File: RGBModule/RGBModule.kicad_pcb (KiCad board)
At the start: 2 copper layers, 17.8 x 24.4 mm, 9 parts, among them P1 CONN_01X03, SW1 Pulsador, SW2 Final_carrera

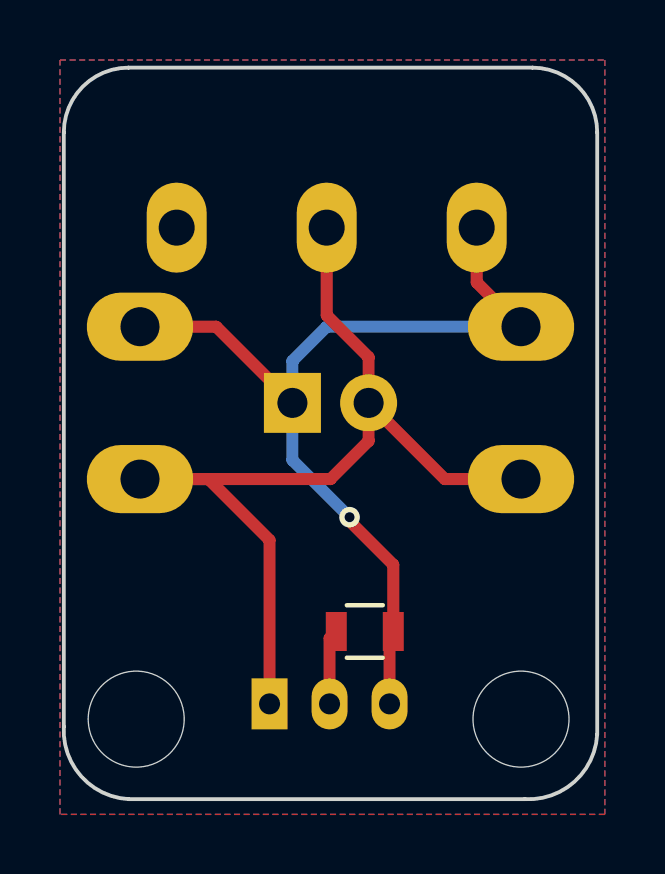
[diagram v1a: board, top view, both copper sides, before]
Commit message: 3D terminado
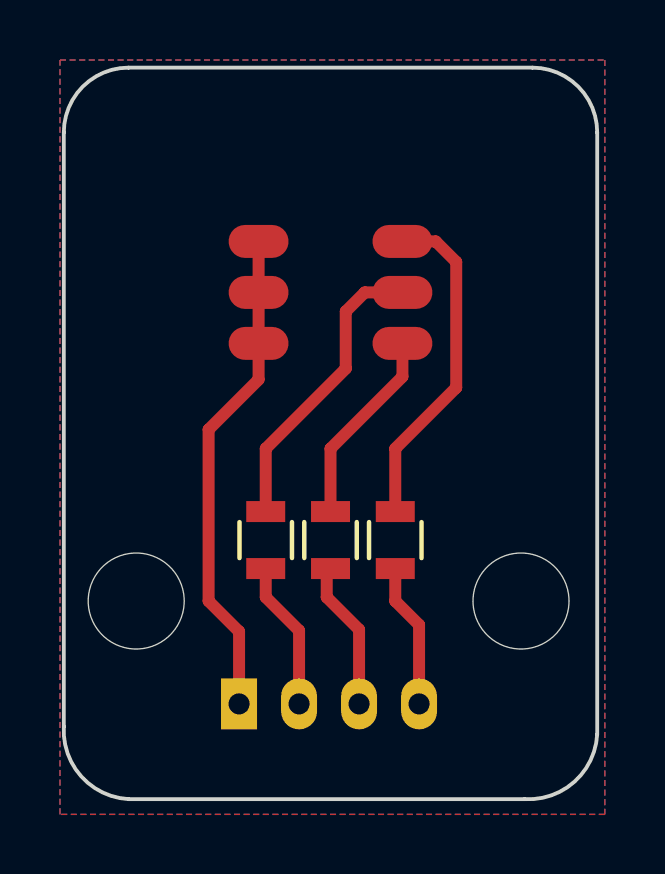
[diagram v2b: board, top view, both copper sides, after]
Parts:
- removed G***: LOGO, logos_frizzy:glance
- removed G***: LOGO, logos_frizzy:web
- removed the REF** at (144.3, 111.9)
- removed the REF** at (131.4, 111.9)
- removed SW1: Pulsador, Buttons_Switches_THT:SW_PUSH-12mm
- removed SW2: Final_carrera, frizzy_switches:limit_sw_tiaihua
- added LED1: RGBLED5050, SparkFun-LED:LED-TRICOLOR-5050, F.Cu at (137.9, 97.7)
- added R3: 470, Resistors_SMD:R_0805, F.Cu at (135.8, 105.9)
- added REF**: MountingHole_3.2mm_M3, Mounting_Holes:MountingHole_3.2mm_M3, F.Cu at (144.3, 108.0)
- added REF**: MountingHole_3.2mm_M3, Mounting_Holes:MountingHole_3.2mm_M3, F.Cu at (131.4, 108.0)
- P1: value CONN_01X03 -> CONN_01X04; footprint Connectors_JST:JST_PH_S3B-PH-K_03x2.00mm_Angled -> Connectors_JST:JST_PH_S4B-PH-K_04x2.00mm_Angled
- R1: value 10k -> 330
- R2: value R_PHOTO -> 330; footprint LEDs:LED-5MM -> Resistors_SMD:R_0805
- moved R2 4.75 mm to (137.9, 105.9), turned to 270 degrees
- moved R1 3.21 mm to (140.1, 105.9), turned to 90 degrees
- moved P1 1.02 mm to (134.9, 111.4)
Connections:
- P1 pad 2: 5V -> RED
- P1 pad 3: SIGNAL -> GREEN
- R1 pad 1: 5V -> BLUE
- R1 pad 2: SIGNAL -> Net-(LED1-Pad3)
- R2 pad 1: SIGNAL -> Net-(LED1-Pad1)
- R2 pad 2: GND -> GREEN
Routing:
- net SIGNAL: track 31.2 -> 0.00 mm, vias 1 -> 0
- net GND: track 33.2 -> 16.5 mm
- net Net-(LED1-Pad3): track 0.00 -> 11.2 mm
- net Net-(LED1-Pad2): track 0.00 -> 9.93 mm
- net Net-(LED1-Pad1): track 0.00 -> 6.60 mm
- net GREEN: track 0.00 -> 5.01 mm
- net RED: track 0.00 -> 4.97 mm
- net BLUE: track 0.00 -> 4.84 mm
- net 5V: track 2.98 -> 0.00 mm

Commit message: Serigrafia añadida
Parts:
- added G***: LOGO, Buzzers_Beepers:logo_rgb, B.Cu at (137.8, 98.4)

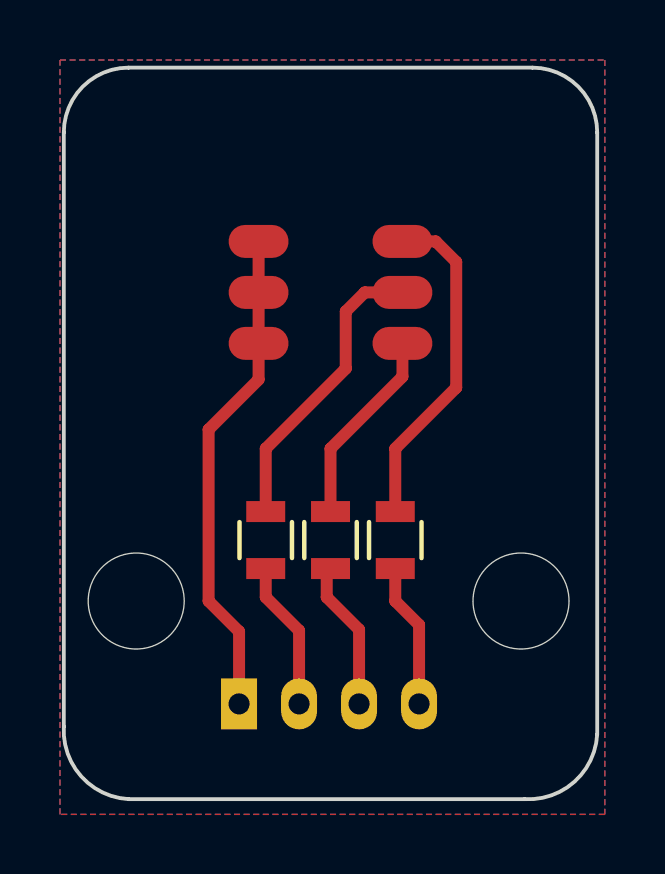
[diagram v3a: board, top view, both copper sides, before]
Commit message: Añadida la serigrafia en la conexiones
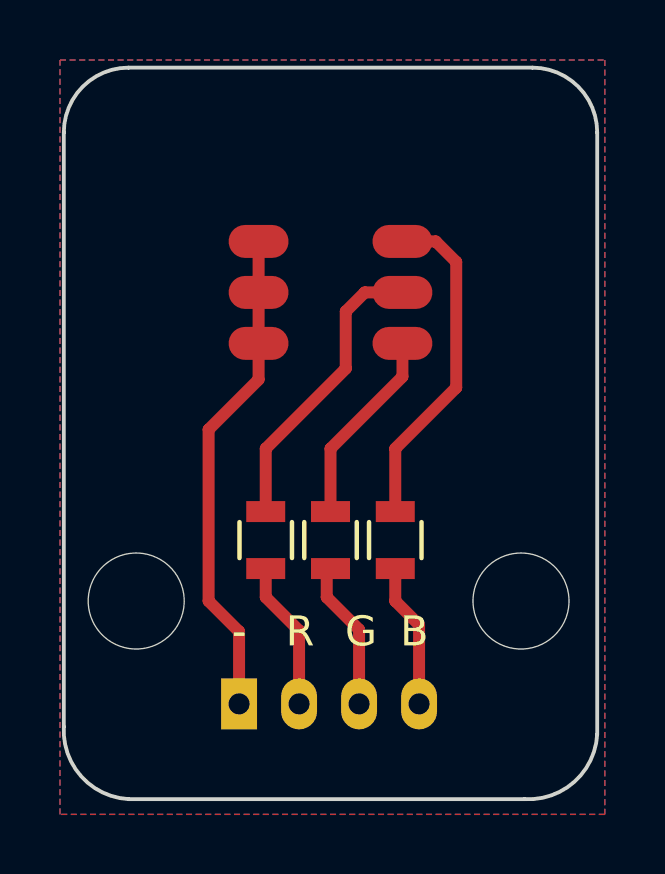
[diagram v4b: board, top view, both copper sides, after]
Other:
- board text added: "-"
- board text added: "B"
- board text added: "G"
- board text added: "R"
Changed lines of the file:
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@@
 (kicad_pcb (version 4) (host pcbnew 4.0.4-stable)
   (general
-    (links 0)
+    (links 9)
     (no_connects 0)
     (area 128.964974 90.106499 146.875501 114.621026)
     (thickness 1.6)
-    (drawings 15)
+    (drawings 19)
     (tracks 30)
     (zones 0)
@@
       (xy -2.827142 5.865992) (xy -2.687518 5.867258) (xy -2.579421 5.867472) (xy -2.074333 5.867258)) (layer B.SilkS) (width 0.01))
   )
+  (gr_text "-\n" (at 134.874 108.966) (layer F.SilkS)
+    (effects (font (size 1 1) (thickness 0.25)))
+  )
+  (gr_text B (at 140.716 108.966) (layer F.SilkS)
+    (effects (font (size 1 1) (thickness 0.25)))
+  )
+  (gr_text "G\n" (at 138.938 108.966) (layer F.SilkS)
+    (effects (font (size 1 1) (thickness 0.25)))
+  )
+  (gr_text R (at 136.906 108.966) (layer F.SilkS)
+    (effects (font (size 1 1) (thickness 0.25)))
+  )
   (dimension 24.384 (width 0.127) (layer Dwgs.User)
